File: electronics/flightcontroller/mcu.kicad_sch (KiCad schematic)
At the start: 28 parts, among them J10 USB, J8 Micro_SD_Card_Det_HYC80-TF08-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, J9 SWD, SW1 RESET, U3 STM32G491CCUx, U6 GT-24-Mini, Y1 24MHz

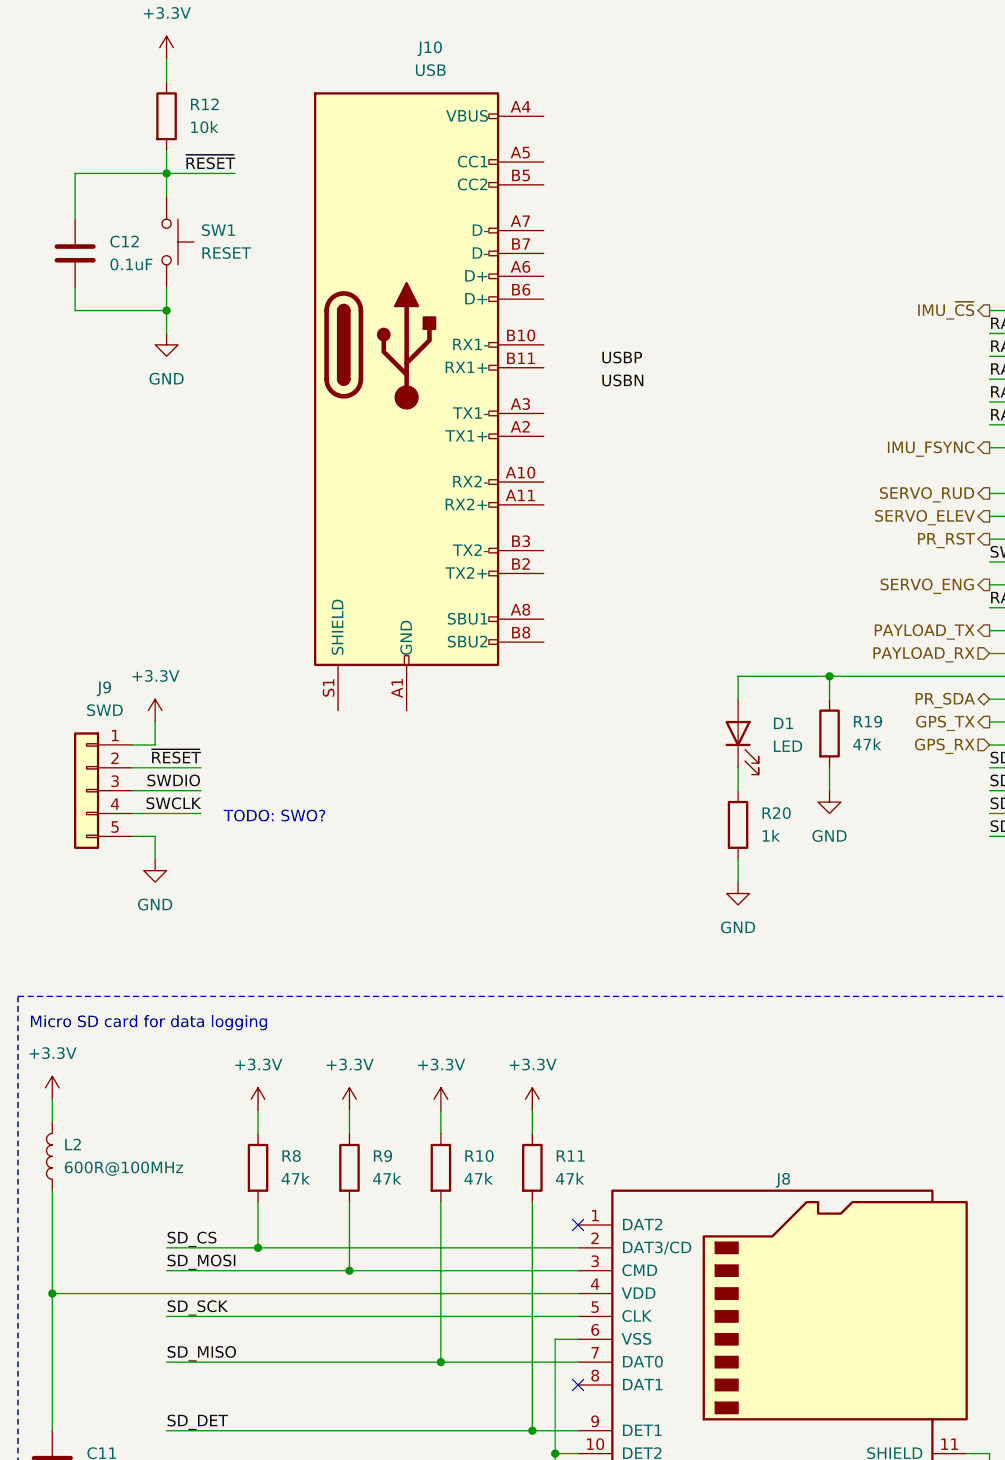
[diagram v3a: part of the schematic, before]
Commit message: electronics: Fix remaining schematics ERC errors.
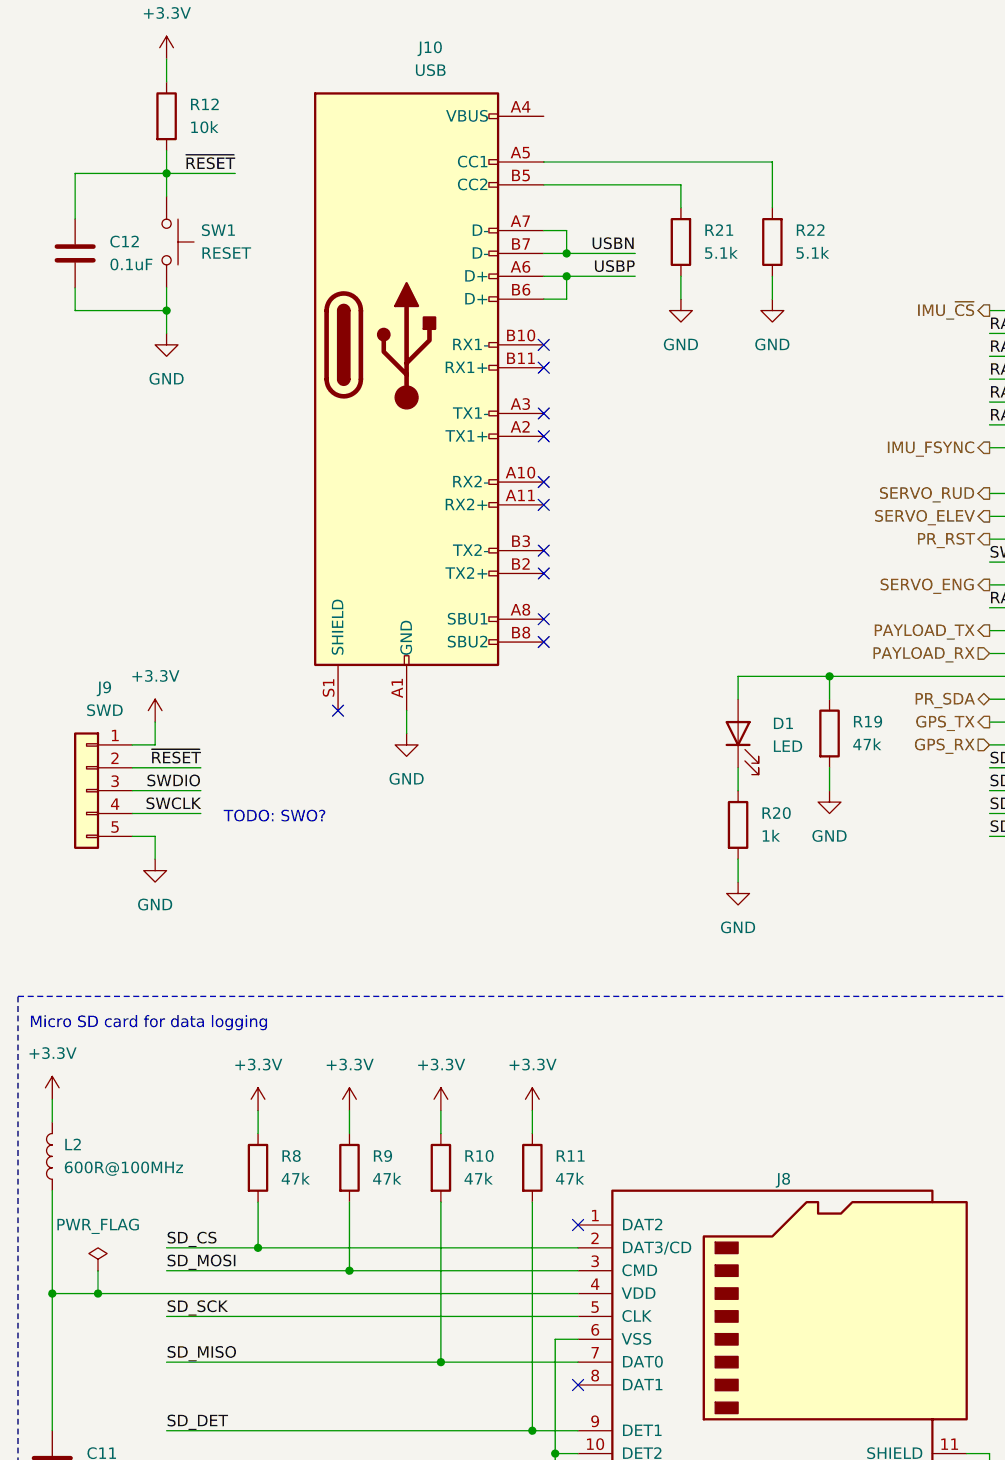
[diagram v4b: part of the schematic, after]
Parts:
- added R21, R22: 5.1k, Resistor_SMD:R_0402_1005Metric, symbol Device:R
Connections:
- net GND: now also J10.A1 (GND), J10.A12 (GND), J10.B1 (GND), J10.B12 (GND), R21.1, R22.1
- net USBN: now also J10.A7 (D-), J10.B7 (D-)
- net USBP: now also J10.A6 (D+), J10.B6 (D+)
- net at J10.A5 (CC1): now also R22.2
- net at J10.B5 (CC2): now also R21.2
- no-connect marks 2 -> 13
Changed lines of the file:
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@@
   (paper "A4")
   (junction (at 19.05 160.02) (diameter 0.9144) (color 0 0 0 0))
+  (junction (at 24.13 160.02) (diameter 0.9144) (color 0 0 0 0))
   (junction (at 31.75 35.56) (diameter 0.9144) (color 0 0 0 0))
   (junction (at 31.75 50.8) (diameter 0.9144) (color 0 0 0 0))
@@
   (junction (at 72.39 175.26) (diameter 0.9144) (color 0 0 0 0))
   (junction (at 74.93 177.8) (diameter 0.9144) (color 0 0 0 0))
+  (junction (at 76.2 44.45) (diameter 0.9144) (color 0 0 0 0))
+  (junction (at 76.2 46.99) (diameter 0.9144) (color 0 0 0 0))
   (junction (at 105.41 91.44) (diameter 0.9144) (color 0 0 0 0))
   (junction (at 140.97 171.45) (diameter 0.9144) (color 0 0 0 0))
@@
   (junction (at 254 34.29) (diameter 0.9144) (color 0 0 0 0))
   (junction (at 266.7 34.29) (diameter 0.9144) (color 0 0 0 0))
+  (no_connect (at 50.8 95.25))
+  (no_connect (at 73.66 54.61))
+  (no_connect (at 73.66 57.15))
+  (no_connect (at 73.66 62.23))
+  (no_connect (at 73.66 64.77))
+  (no_connect (at 73.66 69.85))
+  (no_connect (at 73.66 72.39))
+  (no_connect (at 73.66 77.47))
+  (no_connect (at 73.66 80.01))
+  (no_connect (at 73.66 85.09))
+  (no_connect (at 73.66 87.63))
   (no_connect (at 77.47 152.4))
   (no_connect (at 77.47 170.18))
@@
     (stroke (width 0) (type solid) (color 0 0 0 0))
   )
-  (wire (pts (xy 19.05 160.02) (xy 77.47 160.02))
+  (wire (pts (xy 19.05 160.02) (xy 24.13 160.02))
     (stroke (width 0) (type solid) (color 0 0 0 0))
   )
@@
     (stroke (width 0) (type solid) (color 0 0 0 0))
   )
+  (wire (pts (xy 24.13 157.48) (xy 24.13 160.02))
+    (stroke (width 0) (type solid) (color 0 0 0 0))
+  )
+  (wire (pts (xy 24.13 160.02) (xy 77.47 160.02))
+    (stroke (width 0) (type solid) (color 0 0 0 0))
+  )
   (wire (pts (xy 27.94 99.06) (xy 30.48 99.06))
     (stroke (width 0) (type solid) (color 0 0 0 0))
@@
     (stroke (width 0) (type solid) (color 0 0 0 0))
   )
+  (wire (pts (xy 58.42 95.25) (xy 58.42 97.79))
+    (stroke (width 0) (type solid) (color 0 0 0 0))
+  )
   (wire (pts (xy 62.23 139.7) (xy 62.23 142.24))
     (stroke (width 0) (type solid) (color 0 0 0 0))
@@
     (stroke (width 0) (type solid) (color 0 0 0 0))
   )
+  (wire (pts (xy 73.66 41.91) (xy 76.2 41.91))
+    (stroke (width 0) (type solid) (color 0 0 0 0))
+  )
+  (wire (pts (xy 73.66 44.45) (xy 76.2 44.45))
+    (stroke (width 0) (type solid) (color 0 0 0 0))
+  )
+  (wire (pts (xy 73.66 46.99) (xy 76.2 46.99))
+    (stroke (width 0) (type solid) (color 0 0 0 0))
+  )
+  (wire (pts (xy 73.66 49.53) (xy 76.2 49.53))
+    (stroke (width 0) (type solid) (color 0 0 0 0))
+  )
   (wire (pts (xy 74.93 165.1) (xy 77.47 165.1))
     (stroke (width 0) (type solid) (color 0 0 0 0))
@@
     (stroke (width 0) (type solid) (color 0 0 0 0))
   )
+  (wire (pts (xy 76.2 41.91) (xy 76.2 44.45))
+    (stroke (width 0) (type solid) (color 0 0 0 0))
+  )
+  (wire (pts (xy 76.2 44.45) (xy 83.82 44.45))
+    (stroke (width 0) (type solid) (color 0 0 0 0))
+  )
+  (wire (pts (xy 76.2 46.99) (xy 83.82 46.99))
+    (stroke (width 0) (type solid) (color 0 0 0 0))
+  )
+  (wire (pts (xy 76.2 49.53) (xy 76.2 46.99))
+    (stroke (width 0) (type solid) (color 0 0 0 0))
+  )
   (wire (pts (xy 77.47 175.26) (xy 72.39 175.26))
     (stroke (width 0) (type solid) (color 0 0 0 0))
   )
+  (wire (pts (xy 88.9 36.83) (xy 73.66 36.83))
+    (stroke (width 0) (type solid) (color 0 0 0 0))
+  )
+  (wire (pts (xy 88.9 39.37) (xy 88.9 36.83))
+    (stroke (width 0) (type solid) (color 0 0 0 0))
+  )
+  (wire (pts (xy 88.9 46.99) (xy 88.9 49.53))
+    (stroke (width 0) (type solid) (color 0 0 0 0))
+  )
   (wire (pts (xy 95.25 91.44) (xy 105.41 91.44))
     (stroke (width 0) (type solid) (color 0 0 0 0))
@@
   )
   (wire (pts (xy 95.25 111.76) (xy 95.25 114.3))
+    (stroke (width 0) (type solid) (color 0 0 0 0))
+  )
+  (wire (pts (xy 99.06 34.29) (xy 73.66 34.29))
+    (stroke (width 0) (type solid) (color 0 0 0 0))
+  )
+  (wire (pts (xy 99.06 39.37) (xy 99.06 34.29))
+    (stroke (width 0) (type solid) (color 0 0 0 0))
+  )
+  (wire (pts (xy 99.06 46.99) (xy 99.06 49.53))
     (stroke (width 0) (type solid) (color 0 0 0 0))
   )
@@
     (effects (font (size 1.27 1.27)) (justify right bottom))
   )
-  (label "USBP" (at 80.01 57.15 0)
-    (effects (font (size 1.27 1.27)) (justify left bottom))
-  )
-  (label "USBN" (at 80.01 59.69 0)
-    (effects (font (size 1.27 1.27)) (justify left bottom))
+  (label "USBN" (at 83.82 44.45 180)
+    (effects (font (size 1.27 1.27)) (justify right bottom))
+  )
+  (label "USBP" (at 83.82 46.99 180)
+    (effects (font (size 1.27 1.27)) (justify right bottom))
   )
   (label "RADIO_~{CS}" (at 123.19 53.34 0)
@@
     (pin "1")
   )
+  (symbol (lib_id "power:PWR_FLAG") (at 24.13 157.48 0) (unit 1)
+    (in_bom yes) (on_board yes) (fields_autoplaced)
+    (property "Reference" "#FLG0106" (id 0) (at 24.13 155.575 0)
+      (effects (font (size 1.27 1.27)) hide)
+    )
+    (property "Value" "PWR_FLAG" (id 1) (at 24.13 152.4 0))
+    (property "Footprint" "" (id 2) (at 24.13 157.48 0)
+      (effects (font (size 1.27 1.27)) hide)
+    )
+    (property "Datasheet" "~" (id 3) (at 24.13 157.48 0)
+      (effects (font (size 1.27 1.27)) hide)
+    )
+    (pin "1")
+  )
   (symbol (lib_id "power:GND") (at 19.05 185.42 0) (unit 1)
     (in_bom yes) (on_board yes) (fields_autoplaced)
@@
     (pin "1")
   )
+  (symbol (lib_id "power:GND") (at 58.42 97.79 0) (unit 1)
+    (in_bom yes) (on_board yes) (fields_autoplaced)
+    (property "Reference" "#PWR0146" (id 0) (at 58.42 104.14 0)
+      (effects (font (size 1.27 1.27)) hide)
+    )
+    (property "Value" "GND" (id 1) (at 58.42 102.87 0))
+    (property "Footprint" "" (id 2) (at 58.42 97.79 0)
+      (effects (font (size 1.27 1.27)) hide)
+    )
+    (property "Datasheet" "" (id 3) (at 58.42 97.79 0)
+      (effects (font (size 1.27 1.27)) hide)
+    )
+    (pin "1")
+  )
   (symbol (lib_id "power:GND") (at 74.93 185.42 0) (unit 1)
     (in_bom yes) (on_board yes) (fields_autoplaced)
@@
     (pin "1")
   )
+  (symbol (lib_id "power:GND") (at 88.9 49.53 0) (unit 1)
+    (in_bom yes) (on_board yes) (fields_autoplaced)
+    (property "Reference" "#PWR0147" (id 0) (at 88.9 55.88 0)
+      (effects (font (size 1.27 1.27)) hide)
+    )
+    (property "Value" "GND" (id 1) (at 88.9 54.61 0))
+    (property "Footprint" "" (id 2) (at 88.9 49.53 0)
+      (effects (font (size 1.27 1.27)) hide)
+    )
+    (property "Datasheet" "" (id 3) (at 88.9 49.53 0)
+      (effects (font (size 1.27 1.27)) hide)
+    )
+    (pin "1")
+  )
   (symbol (lib_id "power:GND") (at 95.25 114.3 0) (unit 1)
     (in_bom yes) (on_board yes) (fields_autoplaced)
@@
     (pin "1")
   )
+  (symbol (lib_id "power:GND") (at 99.06 49.53 0) (unit 1)
+    (in_bom yes) (on_board yes) (fields_autoplaced)
+    (property "Reference" "#PWR0148" (id 0) (at 99.06 55.88 0)
+      (effects (font (size 1.27 1.27)) hide)
+    )
+    (property "Value" "GND" (id 1) (at 99.06 54.61 0))
+    (property "Footprint" "" (id 2) (at 99.06 49.53 0)
+      (effects (font (size 1.27 1.27)) hide)
+    )
+    (property "Datasheet" "" (id 3) (at 99.06 49.53 0)
+      (effects (font (size 1.27 1.27)) hide)
+    )
+    (pin "1")
+  )
   (symbol (lib_id "power:GND") (at 105.41 104.14 0) (unit 1)
     (in_bom yes) (on_board yes) (fields_autoplaced)
@@
     (pin "2")
   )
+  (symbol (lib_id "Device:R") (at 88.9 43.18 180) (unit 1)
+    (in_bom yes) (on_board yes) (fields_autoplaced)
+    (property "Reference" "R21" (id 0) (at 91.44 41.9099 0)
+      (effects (font (size 1.27 1.27)) (justify right))
+    )
+    (property "Value" "5.1k" (id 1) (at 91.44 44.4499 0)
+      (effects (font (size 1.27 1.27)) (justify right))
+    )
+    (property "Footprint" "Resistor_SMD:R_0402_1005Metric" (id 2) (at 90.678 43.18 90)
+      (effects (font (size 1.27 1.27)) hide)
+    )
+    (property "Datasheet" "~" (id 3) (at 88.9 43.18 0)
+      (effects (font (size 1.27 1.27)) hide)
+    )
+    (pin "1")
+    (pin "2")
+  )
   (symbol (lib_id "Device:R") (at 95.25 107.95 0) (unit 1)
     (in_bom yes) (on_board yes) (fields_autoplaced)
@@
       (effects (font (size 1.27 1.27)) hide)
     )
+    (pin "1")
+    (pin "2")
+  )
+  (symbol (lib_id "Device:R") (at 99.06 43.18 180) (unit 1)
+    (in_bom yes) (on_board yes) (fields_autoplaced)
+    (property "Reference" "R22" (id 0) (at 101.6 41.9099 0)
+      (effects (font (size 1.27 1.27)) (justify right))
+    )
+    (property "Value" "5.1k" (id 1) (at 101.6 44.4499 0)
+      (effects (font (size 1.27 1.27)) (justify right))
+    )
+    (property "Footprint" "Resistor_SMD:R_0402_1005Metric" (id 2) (at 100.838 43.18 90)
+      (effects (font (size 1.27 1.27)) hide)
+    )
+    (property "Datasheet" "~" (id 3) (at 99.06 43.18 0)
+      (effects (font (size 1.27 1.27)) hide)
+    )

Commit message: electronics: Fixed the reset switch footprint.
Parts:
- SW1: footprint Button_Switch_SMD:SW_SPST_CK_KXT3 -> flightcontroller-footprints:SW_SPST_PTS815; Digikey CKN10778DKR-ND -> (none); Mouser 611-KXT321LHS -> 611-PTS815SJM250SMTR
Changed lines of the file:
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@@
       (effects (font (size 1.27 1.27)) (justify left))
     )
-    (property "Footprint" "Button_Switch_SMD:SW_SPST_CK_KXT3" (id 2) (at 36.83 43.18 0)
+    (property "Footprint" "flightcontroller-footprints:SW_SPST_PTS815" (id 2) (at 36.83 43.18 0)
       (effects (font (size 1.27 1.27)) hide)
     )
@@
       (effects (font (size 1.27 1.27)) hide)
     )
-    (property "Digikey" "CKN10778DKR-ND" (id 4) (at 31.75 43.18 0)
+    (property "Mouser" "611-PTS815SJM250SMTR" (id 5) (at 31.75 43.18 0)
       (effects (font (size 1.27 1.27)) hide)
     )
-    (property "Mouser" " 611-KXT321LHS" (id 5) (at 31.75 43.18 0)
-      (effects (font (size 1.27 1.27)) hide)
-    )

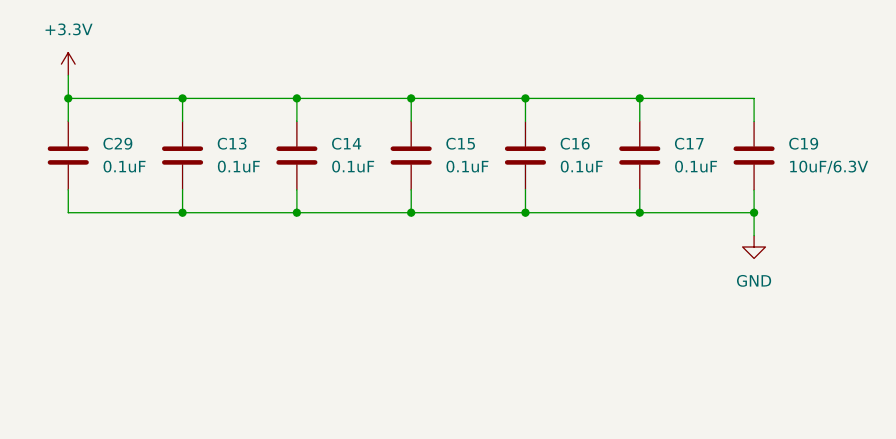
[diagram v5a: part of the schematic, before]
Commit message: electronics: Finished wiring of the flight controller PCB.
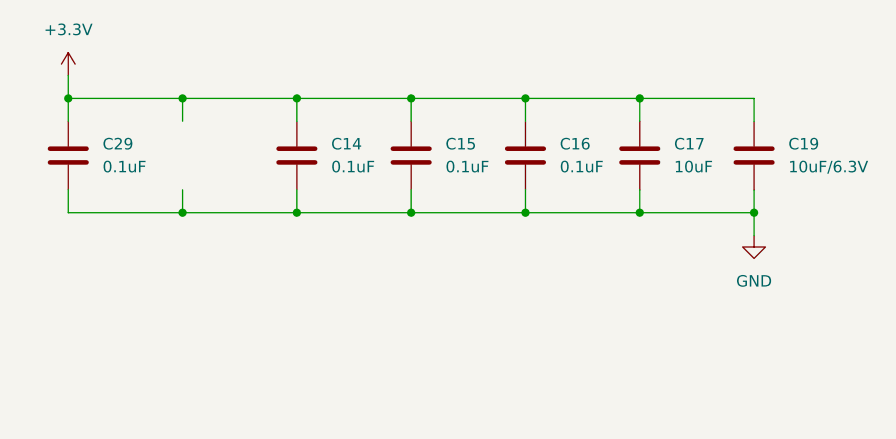
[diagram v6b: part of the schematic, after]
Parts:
- removed C13: 0.1uF, Capacitor_SMD:C_0402_1005Metric, symbol Device:C
- C17: value 0.1uF -> 10uF; Mouser 81-GRM155R71H104KE4D -> 81-GRM155R60J106M05D
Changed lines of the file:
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@@
-    (pin "2")
-  )
-  (symbol (lib_id "Device:C") (at 203.2 27.94 0) (unit 1)
-    (in_bom yes) (on_board yes) (fields_autoplaced)
-    (property "Reference" "C13" (id 0) (at 207.01 26.6699 0)
-      (effects (font (size 1.27 1.27)) (justify left))
-    )
-    (property "Value" "0.1uF" (id 1) (at 207.01 29.2099 0)
-      (effects (font (size 1.27 1.27)) (justify left))
-    )
-    (property "Footprint" "Capacitor_SMD:C_0402_1005Metric" (id 2) (at 204.1652 31.75 0)
-      (effects (font (size 1.27 1.27)) hide)
-    )
-    (property "Datasheet" "~" (id 3) (at 203.2 27.94 0)
-      (effects (font (size 1.27 1.27)) hide)
-    )
-    (property "Mouser" "81-GRM155R71H104KE4D" (id 4) (at 203.2 27.94 0)
-      (effects (font (size 1.27 1.27)) hide)
-    )
-    (pin "1")
     (pin "2")
   )
@@
       (effects (font (size 1.27 1.27)) (justify left))
     )
-    (property "Value" "0.1uF" (id 1) (at 257.81 29.2099 0)
+    (property "Value" "10uF" (id 1) (at 257.81 29.2099 0)
       (effects (font (size 1.27 1.27)) (justify left))
     )
@@
       (effects (font (size 1.27 1.27)) hide)
     )
-    (property "Mouser" "81-GRM155R71H104KE4D" (id 4) (at 254 27.94 0)
+    (property "Mouser" "81-GRM155R60J106M05D" (id 4) (at 254 27.94 0)
       (effects (font (size 1.27 1.27)) hide)
     )

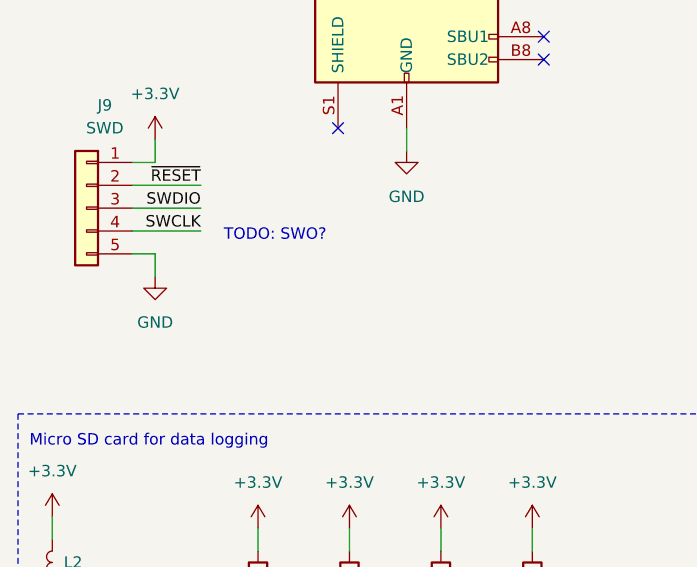
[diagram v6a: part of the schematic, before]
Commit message: electronics: Fixed most flightcontroller DRC errors.
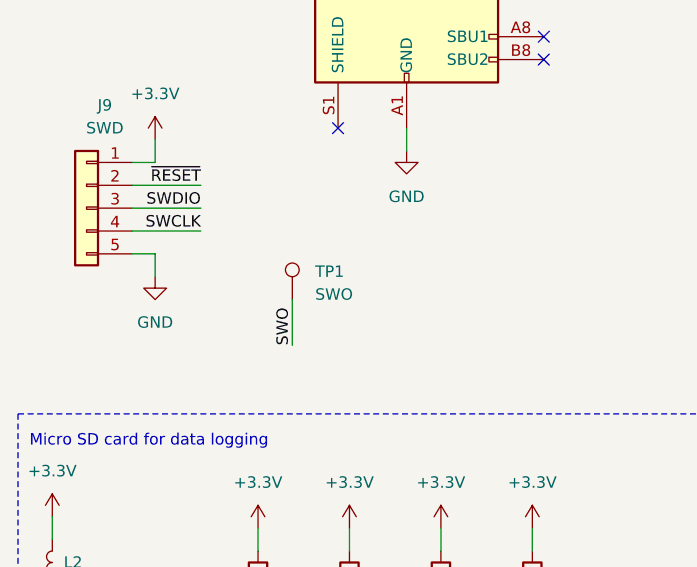
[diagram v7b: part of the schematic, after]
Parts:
- added TP1: SWO, TestPoint:TestPoint_Pad_D2.0mm, symbol Connector:TestPoint
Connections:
- net SWO: now also TP1.1
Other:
- note removed: "TODO: SWO?"
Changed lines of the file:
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@@
+    (stroke (width 0) (type solid) (color 0 0 0 0))
+  )
+  (wire (pts (xy 45.72 114.3) (xy 45.72 119.38))
     (stroke (width 0) (type solid) (color 0 0 0 0))
   )
@@
     (effects (font (size 1.27 1.27)) (justify left bottom))
   )
-  (text "TODO: SWO?" (at 38.1 107.95 0)
-    (effects (font (size 1.27 1.27)) (justify left bottom))
-  )
   (text "Radio" (at 226.06 105.41 0)
     (effects (font (size 1.27 1.27)) (justify left bottom))
@@
   (label "~{RESET}" (at 39.37 35.56 180)
     (effects (font (size 1.27 1.27)) (justify right bottom))
+  )
+  (label "SWO" (at 45.72 119.38 90)
+    (effects (font (size 1.27 1.27)) (justify left bottom))
   )
   (label "USBN" (at 83.82 44.45 180)
@@
       (effects (font (size 1.27 1.27)) hide)
     )
+    (pin "1")
+  )
+  (symbol (lib_id "Connector:TestPoint") (at 45.72 114.3 0) (unit 1)
+    (in_bom yes) (on_board yes) (fields_autoplaced)
+    (property "Reference" "TP1" (id 0) (at 48.26 111.1884 0)
+      (effects (font (size 1.27 1.27)) (justify left))
+    )
+    (property "Value" "SWO" (id 1) (at 48.26 113.7284 0)
+      (effects (font (size 1.27 1.27)) (justify left))
+    )
+    (property "Footprint" "TestPoint:TestPoint_Pad_D2.0mm" (id 2) (at 50.8 114.3 0)
+      (effects (font (size 1.27 1.27)) hide)
+    )
+    (property "Datasheet" "~" (id 3) (at 50.8 114.3 0)
+      (effects (font (size 1.27 1.27)) hide)
+    )
